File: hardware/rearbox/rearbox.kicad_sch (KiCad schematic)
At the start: 22 parts, among them J1 STDC14, J2 ST-LINK, SW1 Reset, U1 LM4040C33FTA, U2 STM32G473RCTx, Y1 48MHz

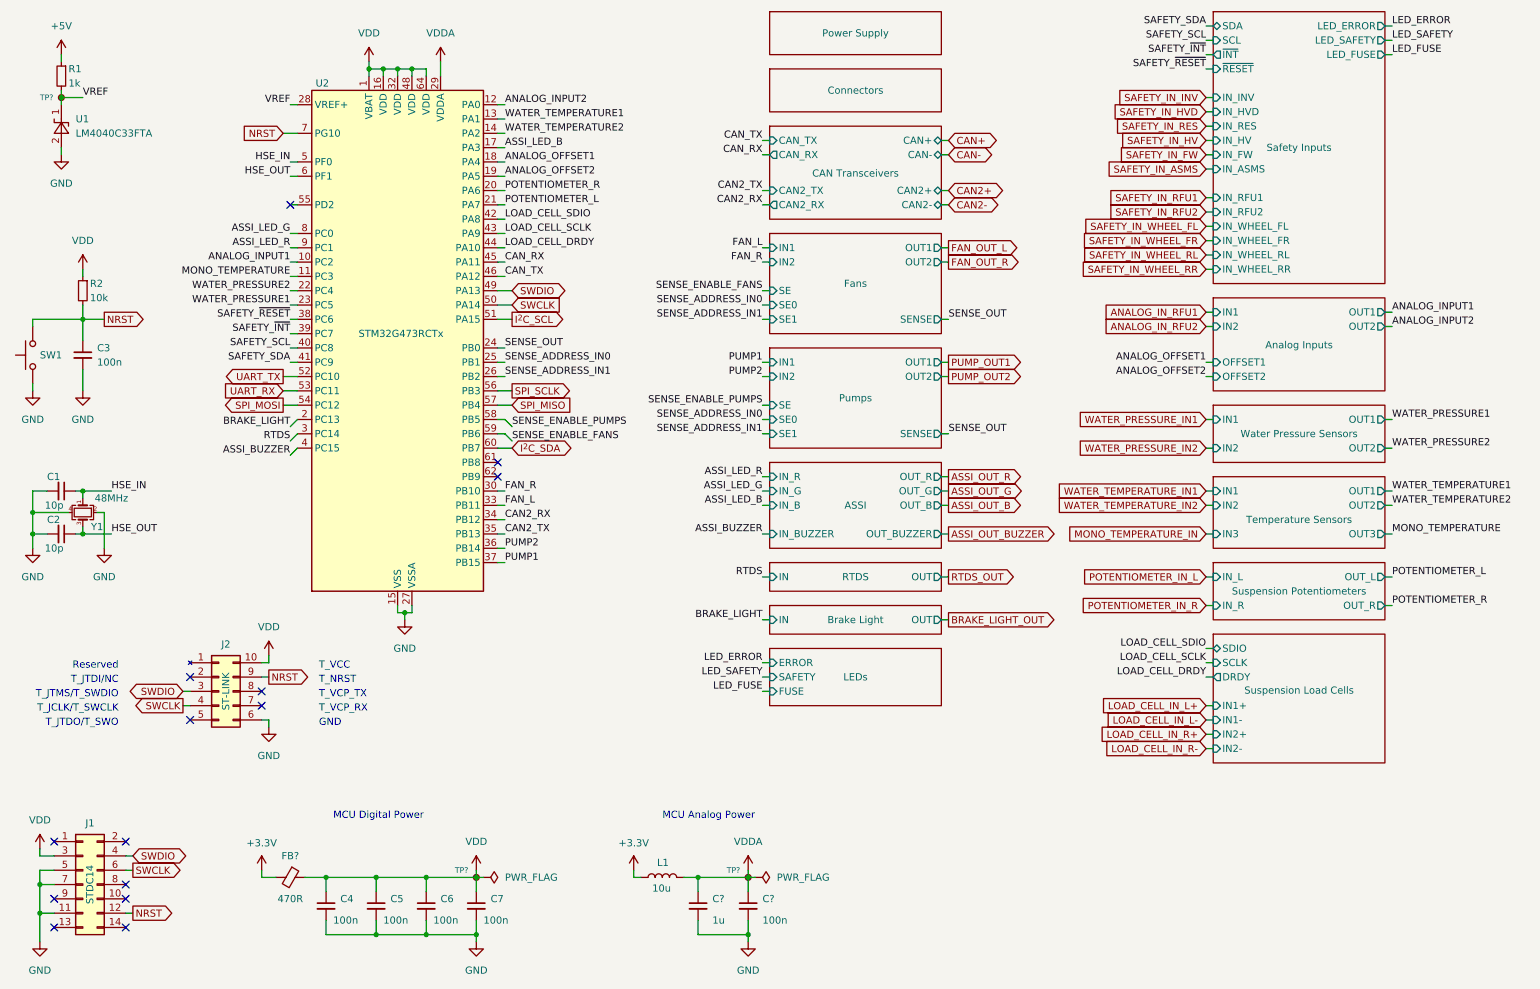
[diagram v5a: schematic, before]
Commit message: Route the tracks on the connector PCB
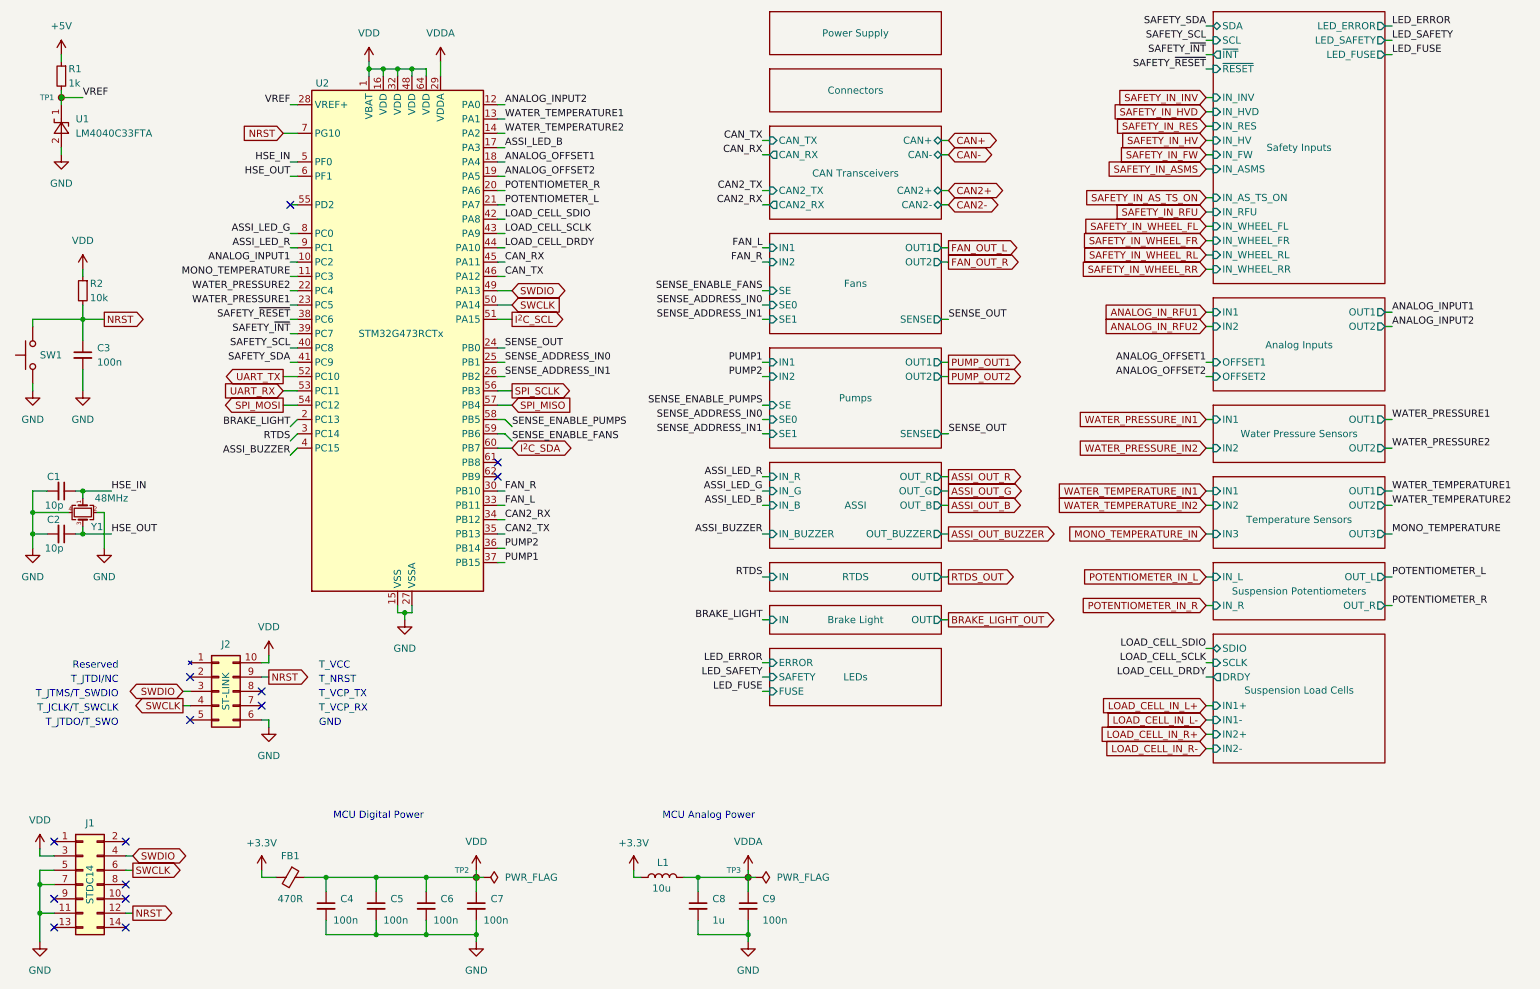
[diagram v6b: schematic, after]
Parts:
- gave numbers to parts that had none: 6
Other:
- sheet Safety Inputs ports: added IN_AS_TS_ON, IN_RFU; removed IN_RFU1, IN_RFU2
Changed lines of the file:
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@@
-    )
-  )
-  (global_label "SAFETY_IN_RFU1" (shape input) (at 227.33 53.34 180) (fields_autoplaced)
-    (effects (font (size 1.27 1.27)) (justify right))
-    (property "Intersheetrefs" "${INTERSHEET_REFS}" (at 209.0632 53.34 0)
-      (effects (font (size 1.27 1.27)) (justify right) hide)
     )
   )
@@
     )
   )
-  (global_label "SAFETY_IN_RFU2" (shape input) (at 227.33 55.88 180) (fields_autoplaced)
-    (effects (font (size 1.27 1.27)) (justify right))
-    (property "Intersheetrefs" "${INTERSHEET_REFS}" (at 209.0632 55.88 0)
+  (global_label "SAFETY_IN_RFU" (shape input) (at 227.33 55.88 180) (fields_autoplaced)
+    (effects (font (size 1.27 1.27)) (justify right))
+    (property "Intersheetrefs" "${INTERSHEET_REFS}" (at 210.1933 55.88 0)
       (effects (font (size 1.27 1.27)) (justify right) hide)
     )
@@
     (effects (font (size 1.27 1.27)) (justify right))
     (property "Intersheetrefs" "${INTERSHEET_REFS}" (at 52.7928 85.09 0)
+      (effects (font (size 1.27 1.27)) (justify right) hide)
+    )
+  )
+  (global_label "SAFETY_IN_AS_TS_ON" (shape input) (at 227.33 53.34 180) (fields_autoplaced)
+    (effects (font (size 1.27 1.27) (color 179 0 27 1)) (justify right))
+    (property "Intersheetrefs" "${INTERSHEET_REFS}" (at 204.811 53.34 0)
       (effects (font (size 1.27 1.27)) (justify right) hide)
     )
@@
   (symbol (lib_id "Device:FerriteBead_Small") (at 64.77 173.99 270) (unit 1)
     (in_bom yes) (on_board yes) (dnp no)
-    (property "Reference" "FB?" (at 64.77 170.18 90)
+    (property "Reference" "FB1" (at 64.77 170.18 90)
       (effects (font (size 1.27 1.27)))
     )
@@
     (instances
       (project "rearbox"
-        (path "/b652b05a-4e3d-4ad1-b032-18886abe7d45/38408e41-dfb1-4c27-acb0-3f1224cc8789"
-          (reference "FB?") (unit 1)
-        )
-        (path "/b652b05a-4e3d-4ad1-b032-18886abe7d45/38408e41-dfb1-4c27-acb0-3f1224cc8789/eec2c93a-0fce-4d3a-ab43-9e1e0481c06c"
-          (reference "FB3") (unit 1)
-        )
-        (path "/b652b05a-4e3d-4ad1-b032-18886abe7d45/38408e41-dfb1-4c27-acb0-3f1224cc8789/f1ed15a3-9302-436f-b25a-713477aeadf3"
-          (reference "FB1") (unit 1)
-        )
-        (path "/b652b05a-4e3d-4ad1-b032-18886abe7d45/5d9671f9-6e77-4376-b4d6-afe9f66a07c2"
-          (reference "FB5") (unit 1)
-        )
         (path "/b652b05a-4e3d-4ad1-b032-18886abe7d45"
           (reference "FB1") (unit 1)
@@
   (symbol (lib_id "power:+5V") (at 24.13 27.94 0) (unit 1)
     (in_bom yes) (on_board yes) (dnp no)
-    (property "Reference" "#PWR041" (at 24.13 31.75 0)
+    (property "Reference" "#PWR05" (at 24.13 31.75 0)
       (effects (font (size 1.27 1.27)) hide)
     )
@@
     (instances
       (project "rearbox"
-        (path "/b652b05a-4e3d-4ad1-b032-18886abe7d45/7045152e-d7a2-42d7-9b15-138e7f2928ca"
-          (reference "#PWR041") (unit 1)
-        )
         (path "/b652b05a-4e3d-4ad1-b032-18886abe7d45"
           (reference "#PWR05") (unit 1)
@@
   (symbol (lib_id "Device:C_Small") (at 137.16 179.07 0) (unit 1)
     (in_bom yes) (on_board yes) (dnp no)
-    (property "Reference" "C?" (at 139.7 177.8 0)
+    (property "Reference" "C8" (at 139.7 177.8 0)
       (effects (font (size 1.27 1.27)) (justify left))
     )
@@
     (instances
       (project "rearbox"
-        (path "/b652b05a-4e3d-4ad1-b032-18886abe7d45/7045152e-d7a2-42d7-9b15-138e7f2928ca"
-          (reference "C?") (unit 1)
-        )
         (path "/b652b05a-4e3d-4ad1-b032-18886abe7d45"
           (reference "C8") (unit 1)
@@
   (symbol (lib_id "Connector:TestPoint_Small") (at 146.05 173.99 0) (unit 1)
     (in_bom yes) (on_board yes) (dnp no)
-    (property "Reference" "TP?" (at 142.24 172.72 0)
+    (property "Reference" "TP3" (at 142.24 172.72 0)
       (effects (font (size 1 1)) (justify left))
     )
@@
     (instances
       (project "rearbox"
-        (path "/b652b05a-4e3d-4ad1-b032-18886abe7d45/38408e41-dfb1-4c27-acb0-3f1224cc8789"
-          (reference "TP?") (unit 1)
-        )
-        (path "/b652b05a-4e3d-4ad1-b032-18886abe7d45/38408e41-dfb1-4c27-acb0-3f1224cc8789/eec2c93a-0fce-4d3a-ab43-9e1e0481c06c"
-          (reference "TP3") (unit 1)
-        )
-        (path "/b652b05a-4e3d-4ad1-b032-18886abe7d45/38408e41-dfb1-4c27-acb0-3f1224cc8789/f1ed15a3-9302-436f-b25a-713477aeadf3"
-          (reference "TP1") (unit 1)
-        )
-        (path "/b652b05a-4e3d-4ad1-b032-18886abe7d45/562e38ba-d94a-4627-8fa0-e9eb7b5e4e9a"
-          (reference "TP49") (unit 1)
-        )
         (path "/b652b05a-4e3d-4ad1-b032-18886abe7d45"
           (reference "TP3") (unit 1)
@@
   (symbol (lib_id "Device:C_Small") (at 146.05 179.07 0) (unit 1)
     (in_bom yes) (on_board yes) (dnp no)
-    (property "Reference" "C?" (at 148.59 177.8 0)
+    (property "Reference" "C9" (at 148.59 177.8 0)
       (effects (font (size 1.27 1.27)) (justify left))
     )
@@
     (instances
       (project "rearbox"
-        (path "/b652b05a-4e3d-4ad1-b032-18886abe7d45/7045152e-d7a2-42d7-9b15-138e7f2928ca"
-          (reference "C?") (unit 1)
-        )
         (path "/b652b05a-4e3d-4ad1-b032-18886abe7d45"
           (reference "C9") (unit 1)
@@
   (symbol (lib_id "Connector:TestPoint_Small") (at 97.79 173.99 0) (unit 1)
     (in_bom yes) (on_board yes) (dnp no)
-    (property "Reference" "TP?" (at 93.98 172.72 0)
+    (property "Reference" "TP2" (at 93.98 172.72 0)
       (effects (font (size 1 1)) (justify left))
     )
@@
     (instances
       (project "rearbox"
-        (path "/b652b05a-4e3d-4ad1-b032-18886abe7d45/38408e41-dfb1-4c27-acb0-3f1224cc8789"
-          (reference "TP?") (unit 1)
-        )
-        (path "/b652b05a-4e3d-4ad1-b032-18886abe7d45/38408e41-dfb1-4c27-acb0-3f1224cc8789/eec2c93a-0fce-4d3a-ab43-9e1e0481c06c"
-          (reference "TP3") (unit 1)
-        )
-        (path "/b652b05a-4e3d-4ad1-b032-18886abe7d45/38408e41-dfb1-4c27-acb0-3f1224cc8789/f1ed15a3-9302-436f-b25a-713477aeadf3"
-          (reference "TP1") (unit 1)
-        )
-        (path "/b652b05a-4e3d-4ad1-b032-18886abe7d45/562e38ba-d94a-4627-8fa0-e9eb7b5e4e9a"
-          (reference "TP49") (unit 1)
-        )
         (path "/b652b05a-4e3d-4ad1-b032-18886abe7d45"
           (reference "TP2") (unit 1)
@@
   (symbol (lib_id "Connector:TestPoint_Small") (at 24.13 35.56 0) (unit 1)
     (in_bom yes) (on_board yes) (dnp no)
-    (property "Reference" "TP?" (at 20.32 35.56 0)
+    (property "Reference" "TP1" (at 20.32 35.56 0)
       (effects (font (size 1 1)) (justify left))
     )
@@
     (instances
       (project "rearbox"
-        (path "/b652b05a-4e3d-4ad1-b032-18886abe7d45/38408e41-dfb1-4c27-acb0-3f1224cc8789"
-          (reference "TP?") (unit 1)
-        )
-        (path "/b652b05a-4e3d-4ad1-b032-18886abe7d45/38408e41-dfb1-4c27-acb0-3f1224cc8789/eec2c93a-0fce-4d3a-ab43-9e1e0481c06c"
-          (reference "TP3") (unit 1)
-        )
-        (path "/b652b05a-4e3d-4ad1-b032-18886abe7d45/38408e41-dfb1-4c27-acb0-3f1224cc8789/f1ed15a3-9302-436f-b25a-713477aeadf3"
-          (reference "TP1") (unit 1)
-        )
-        (path "/b652b05a-4e3d-4ad1-b032-18886abe7d45/562e38ba-d94a-4627-8fa0-e9eb7b5e4e9a"
-          (reference "TP49") (unit 1)
-        )
         (path "/b652b05a-4e3d-4ad1-b032-18886abe7d45"
           (reference "TP1") (unit 1)
@@
       (effects (font (size 1.27 1.27)) (justify left))
     )
-    (pin "IN_RFU2" input (at 228.6 55.88 180)
+    (pin "IN_RFU" input (at 228.6 55.88 180)
       (effects (font (size 1.27 1.27)) (justify left))
     )
@@
       (effects (font (size 1.27 1.27)) (justify left))
     )
-    (pin "IN_RFU1" input (at 228.6 53.34 180)
-      (effects (font (size 1.27 1.27)) (justify left))
-    )
+    (pin "IN_AS_TS_ON" input (at 228.6 53.34 180)
+      (effects (font (size 1.27 1.27)) (justify left))
+    )
